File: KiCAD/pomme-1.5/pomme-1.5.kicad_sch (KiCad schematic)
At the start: 33 parts, among them SW1 RESET, SW2 single step, SW3 step, U12 74HC138, U2 74HC04, U3 74HC74, U7 74HC00, Y1 3.6864Mhz

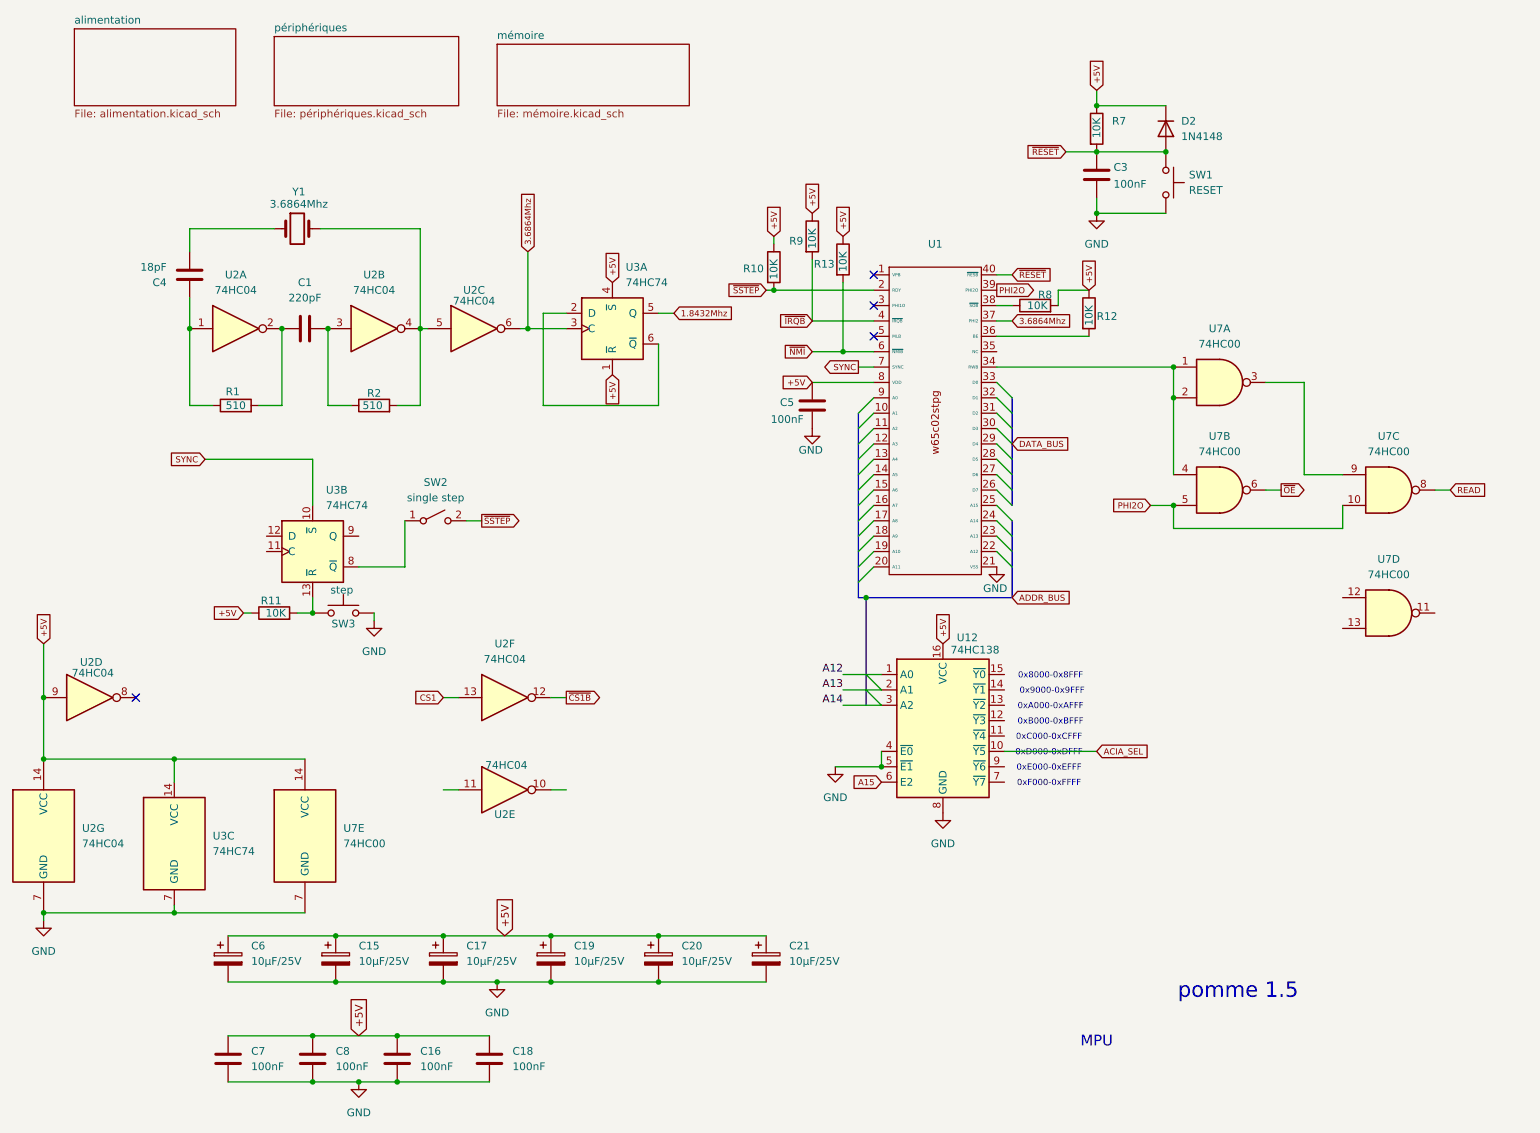
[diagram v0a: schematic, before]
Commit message: Modification de test1.s et de la schématique. L'ordinateur fonctionne à 3.68Mhz
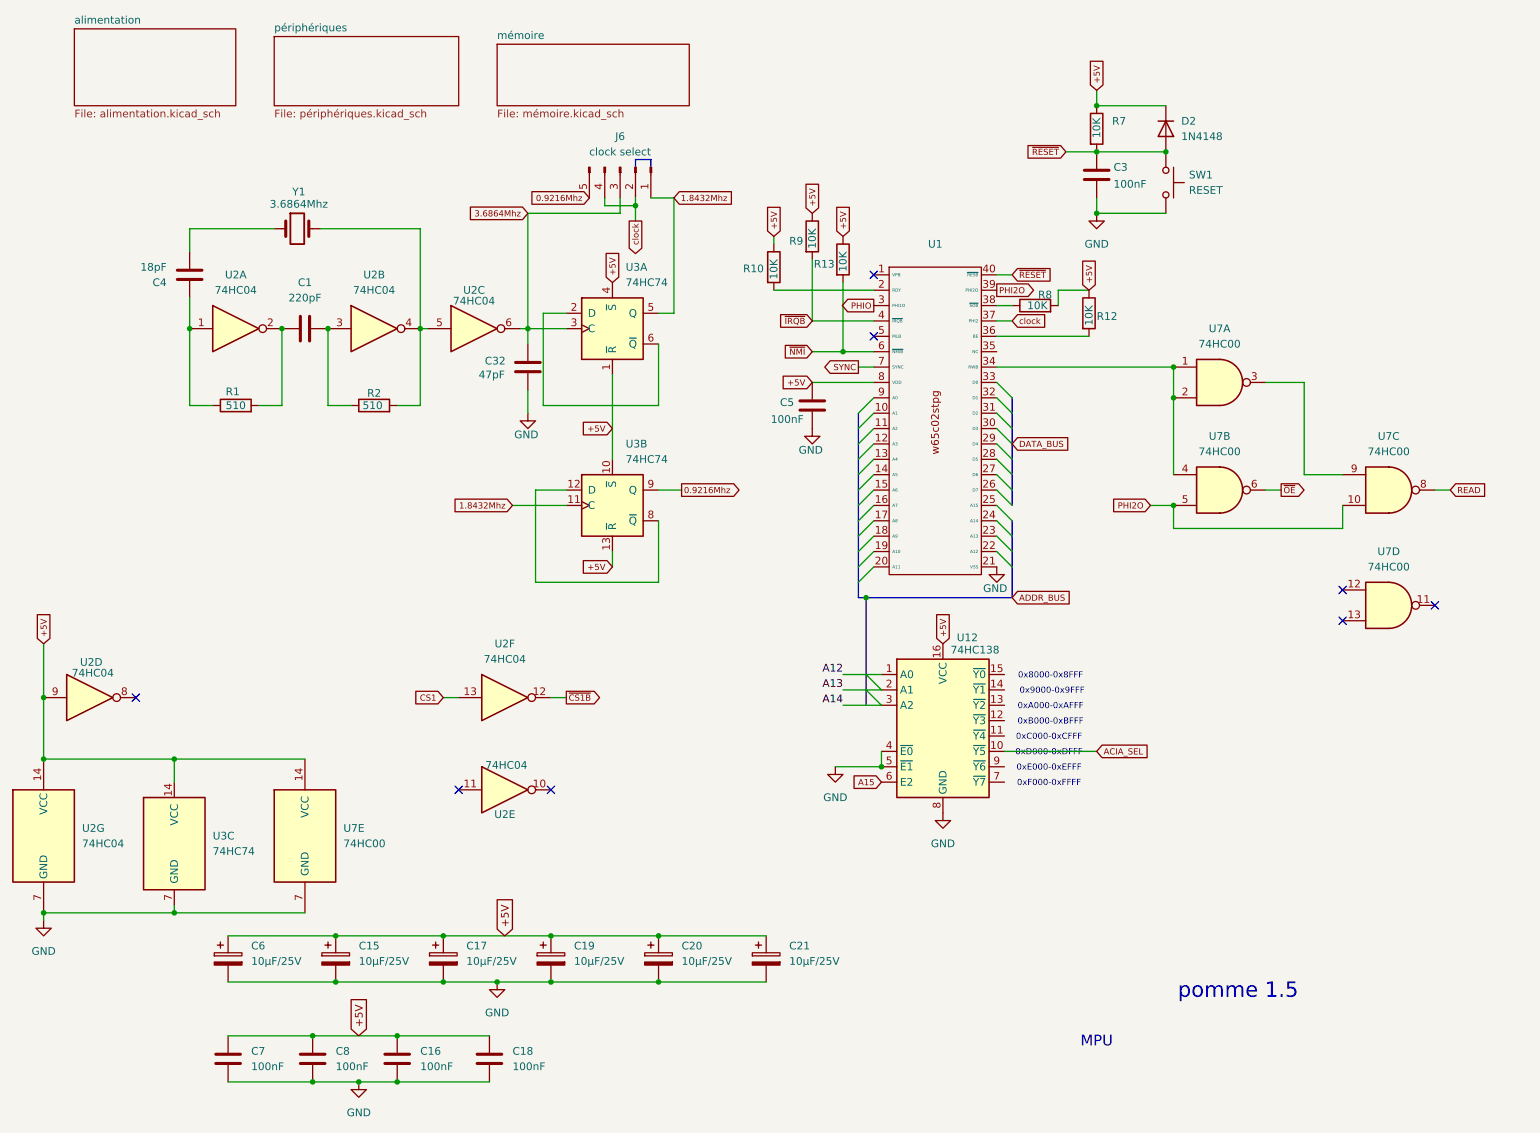
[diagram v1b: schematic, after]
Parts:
- removed R11: 10K, symbol Device:R
- removed SW2: single step, symbol Switch:SW_SPST
- removed SW3: step, symbol Switch:SW_Push
- added C32: 47pF, symbol Device:C
- added J6: clock select, symbol Connector:Conn_01x05_Pin
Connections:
- net +5V: now also U3.10 (~{S}), U3.13 (~{R})
- net 1.8432Mhz: now also U3.11 (C), J6.1 (Pin_1)
- net 3.6864Mhz: now also C32.2, J6.3 (Pin_3); no longer U1.37 (PHI2)
- net GND: now also C32.1
- net SYNC: no longer U3.10 (~{S})
- net PHIO: now reaches U1.3 (PHI1O)
- net at U3.12 (D): now also U3.8 (~{Q})
- net 0.9216Mhz: now reaches U3.9 (Q)
- net 0.9216Mhz: now also J6.5 (Pin_5)
- net ~{SSTEP}: no longer names the net of R10.2, U1.2 (RDY)
- new net clock: J6.2 (Pin_2), J6.4 (Pin_4), U1.37 (PHI2)
- no-connect marks 4 -> 8
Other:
- moved on the sheet: U3B, U7D

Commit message: Complété schématique alimentation
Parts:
- added D1: POWER, symbol Device:LED
- added R4: R, symbol Device:R
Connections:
- net +5V: now also D1.2 (A)
- net GND: now also R4.2
- new net: D1.1 (K), R4.1

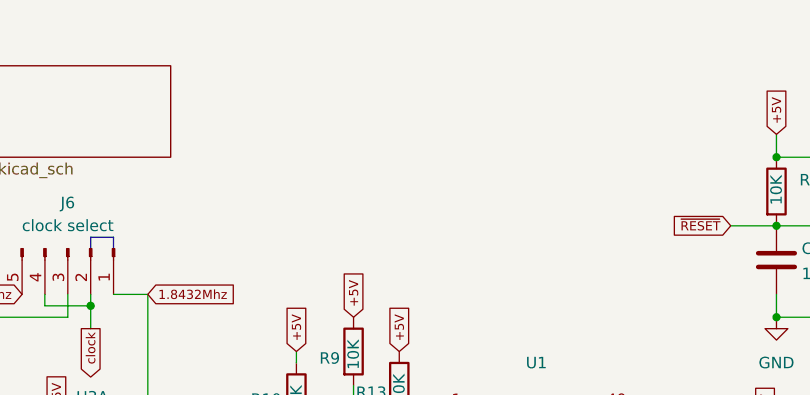
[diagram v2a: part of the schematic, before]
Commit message: Ajout du sous-projet p1+_drive
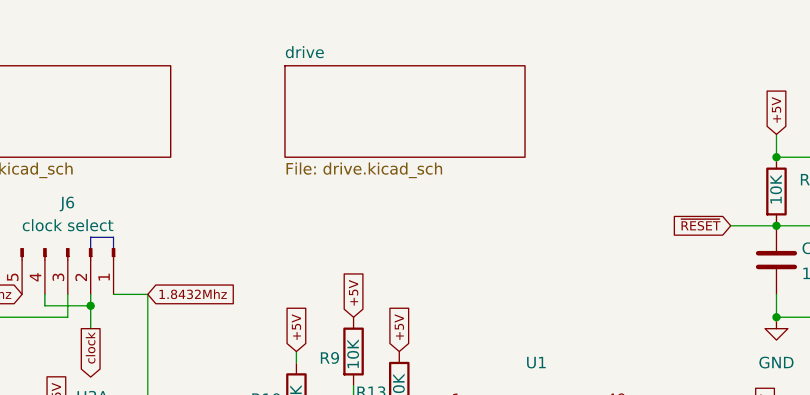
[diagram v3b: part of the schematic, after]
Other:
- added sheet drive (drive.kicad_sch)
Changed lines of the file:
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@@
+		)
+	)
+	(sheet
+		(at 137.16 19.05)
+		(size 26.67 10.16)
+		(fields_autoplaced yes)
+		(stroke
+			(width 0.1524)
+			(type solid)
+		)
+		(fill
+			(color 0 0 0 0.0000)
+		)
+		(property "Sheetname" "drive"
+			(at 137.16 18.3384 0)
+			(effects
+				(font
+					(size 1.27 1.27)
+				)
+				(justify left bottom)
+			)
+		)
+		(property "Sheetfile" "drive.kicad_sch"
+			(at 137.16 29.7946 0)
+			(effects
+				(font
+					(size 1.27 1.27)
+				)
+				(justify left top)
+			)
+		)
+		(instances
+			(project "pomme-1.5"
+				(path "/46a37b86-f1f5-4cd9-9809-f219c84ab6f2"
+					(page "5")
+				)
+			)
 		)
 	)

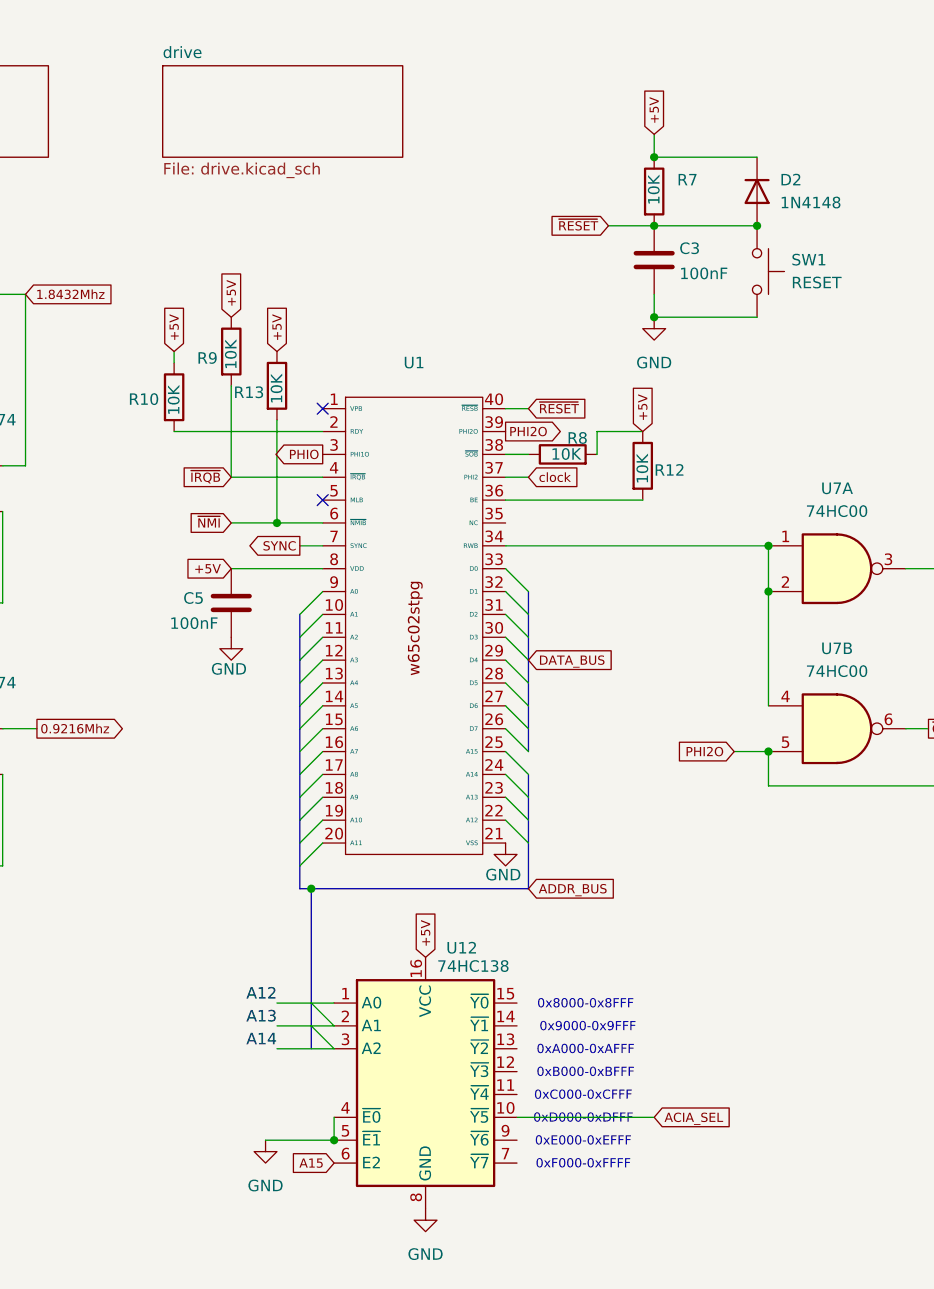
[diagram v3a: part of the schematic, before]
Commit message: Remplacement du p1+ drive par un circuit différent et modication à p1+ terminal et au pomme 1+
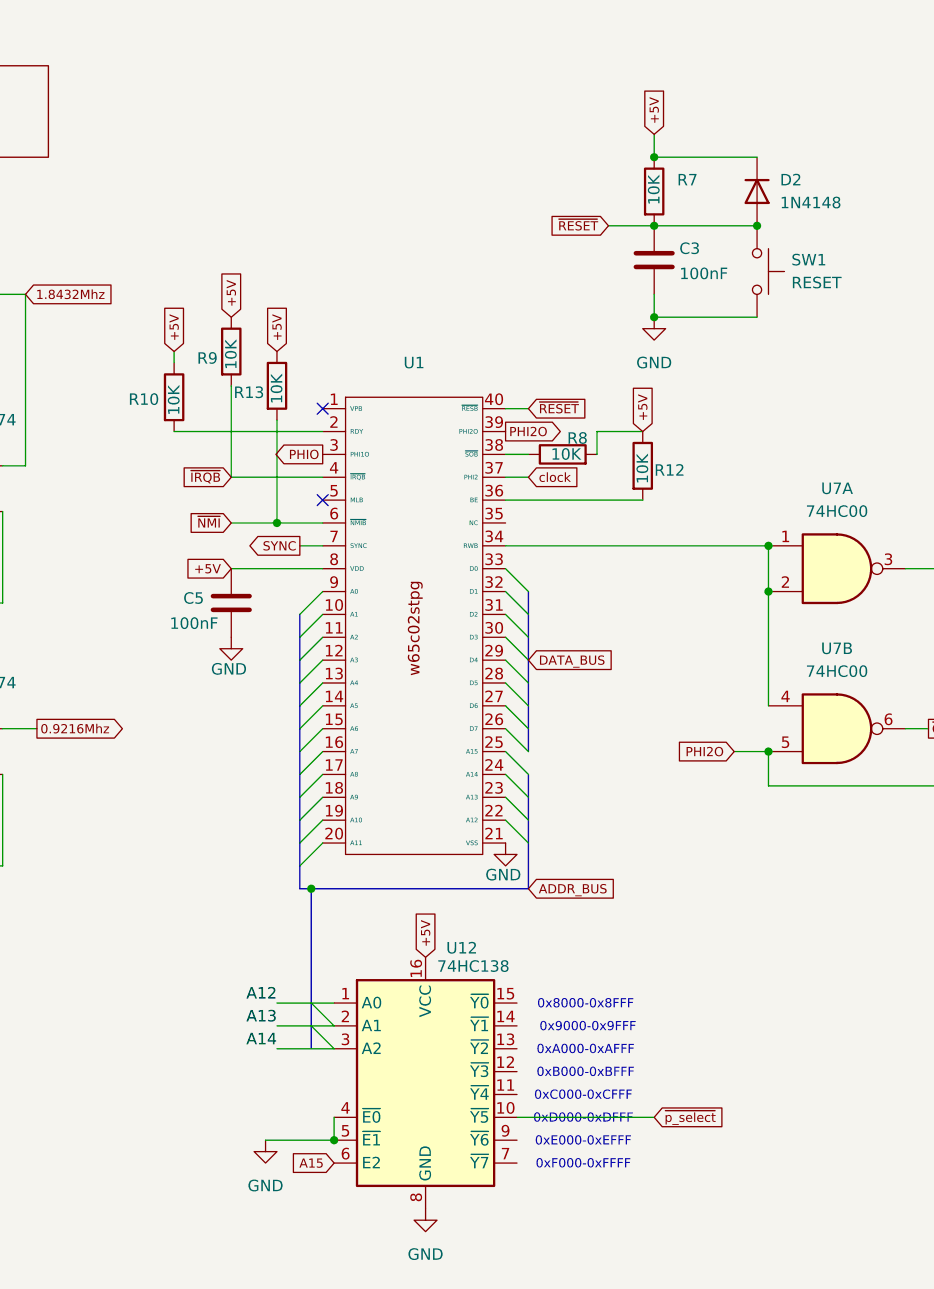
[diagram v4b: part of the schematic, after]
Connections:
- net ACIA_SEL renamed ~{p_select}
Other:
- removed sheet drive
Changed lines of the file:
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@@
 		)
 	)
-	(global_label "ACIA_SEL"
+	(global_label "~{p_select}"
 		(shape input)
 		(at 191.77 135.89 0)
@@
 		)
 		(property "Intersheetrefs" "${INTERSHEET_REFS}"
-			(at 200.8829 135.89 0)
+			(at 200.3992 135.89 0)
 			(effects
 				(font
@@
 				)
 			)
-		)
-	)
-	(sheet
-		(at 137.16 19.05)
-		(size 26.67 10.16)
-		(fields_autoplaced yes)
-		(stroke
-			(width 0.1524)
-			(type solid)
-		)
-		(fill
-			(color 0 0 0 0.0000)
-		)
-		(property "Sheetname" "drive"
-			(at 137.16 18.3384 0)
-			(effects
-				(font
-					(size 1.27 1.27)
-				)
-				(justify left bottom)
-			)
-		)
-		(property "Sheetfile" "drive.kicad_sch"
-			(at 137.16 29.7946 0)
-			(effects
-				(font
-					(size 1.27 1.27)
-				)
-				(justify left top)
-			)
-		)
-		(instances
-			(project "pomme-1.5"
-				(path "/46a37b86-f1f5-4cd9-9809-f219c84ab6f2"
-					(page "5")
-				)
-			)
